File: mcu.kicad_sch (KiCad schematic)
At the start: 33 parts, among them J11 Conn_02x05_Odd_Even, J2 Conn_01x10, J3 Conn_01x10, J4 Conn_02x05_Odd_Even, U5 REF3033, U7 STM32F407VGTx, Y1 8MHz

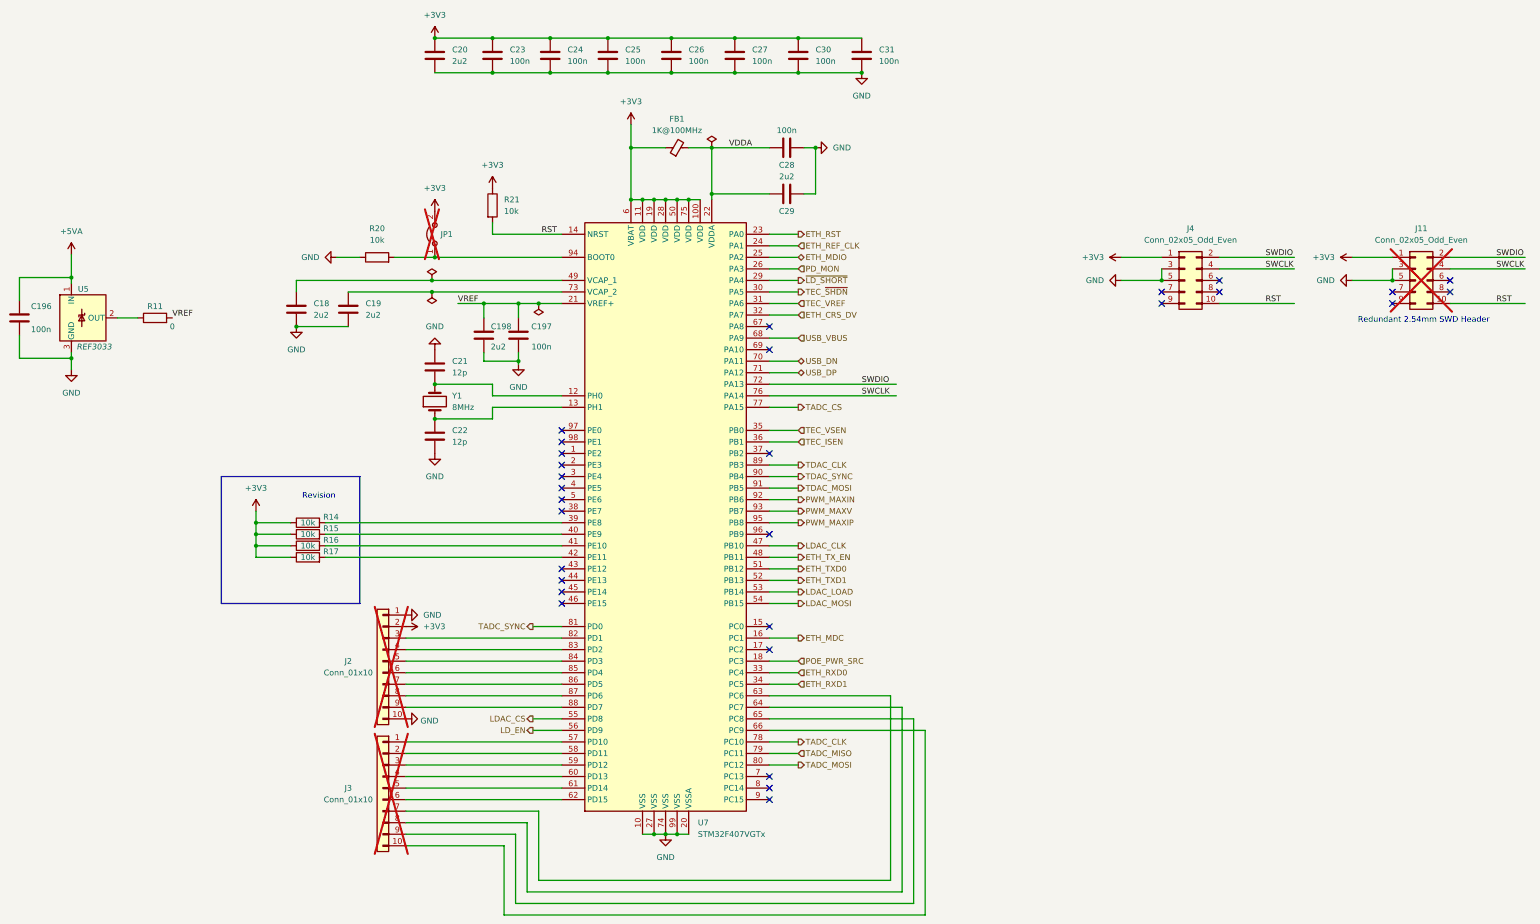
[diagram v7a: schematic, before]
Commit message: pcb: Finish Layout for rev0_3 - Assign MFR_PN for all Components - schematics changes:   - drivestage: Add Switch to optionally enable Modulation Signal Termination   -             Add alternate Precision Power Resistor   -             Modify the RC network values at TIA LPF Output   - MCU: Add Redundant 2.54mm pitch Programming Header   - thermostat: Duplicate the power filter network for alternate Temperature ADC
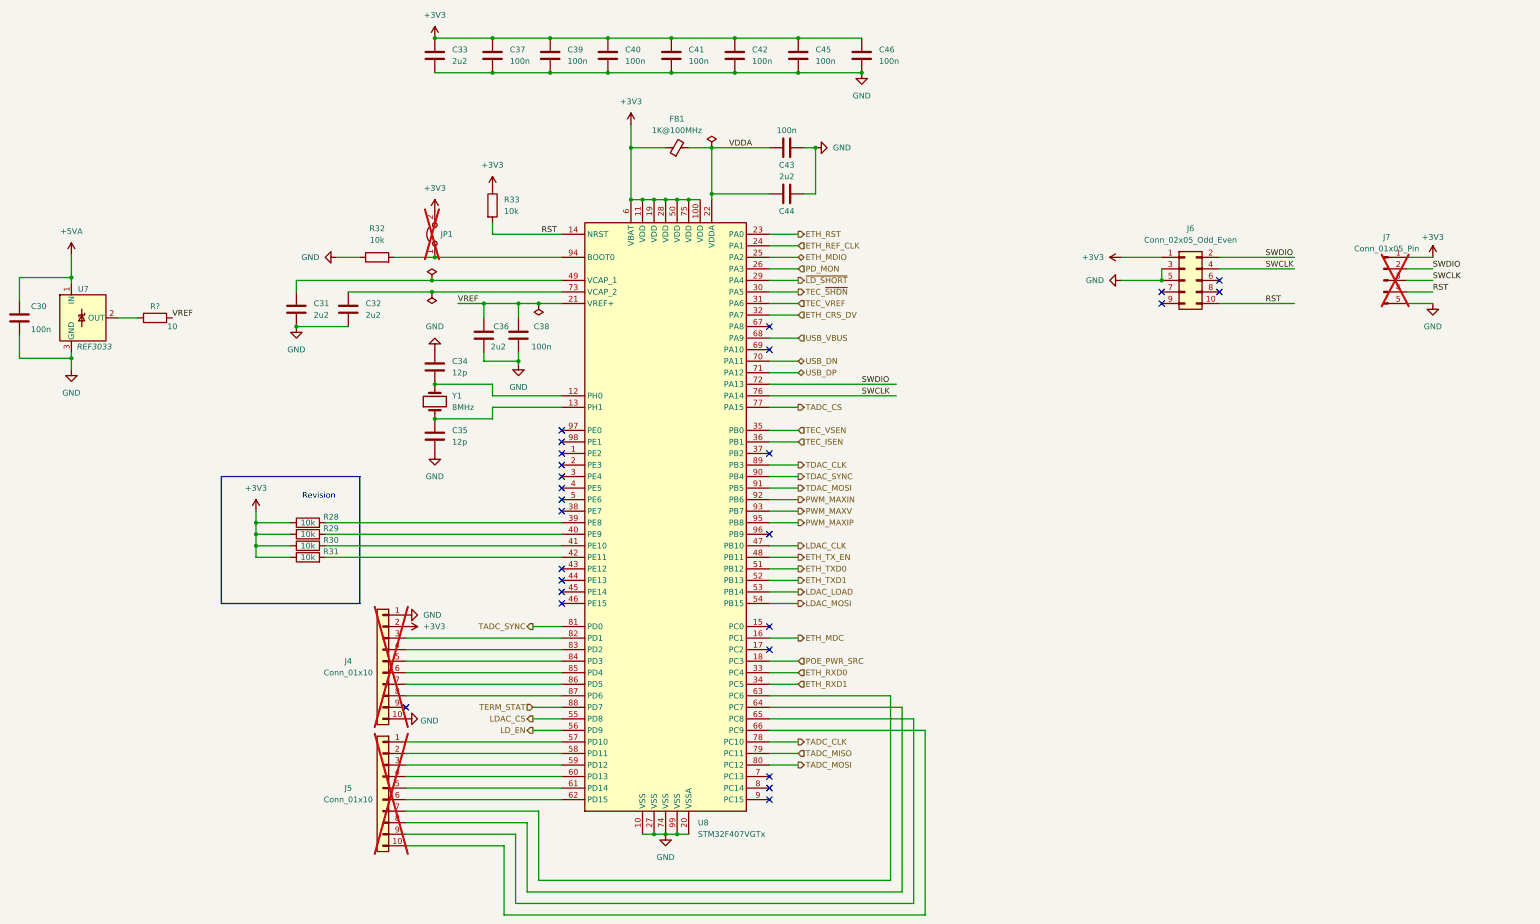
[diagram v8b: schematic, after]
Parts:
- removed J11: Conn_02x05_Odd_Even, Connector_PinHeader_2.54mm:PinHeader_2x05_P2.54mm_Vertical, symbol Connector_Generic:Conn_02x05_Odd_Even
- added J7: Conn_01x05_Pin, Connector_PinHeader_2.54mm:PinHeader_1x05_P2.54mm_Vertical, symbol Connector:Conn_01x05_Pin
- R?: renamed from R11; value 0 -> 10; MFR_PN RMCF0603ZT0R00 -> RT0603BRD0710RL; MFR_PN_ALT CR0603-J/-000ELF -> WR06X10R0FTL
- renumbered C196 to C30, C18 to C31, C19 to C32, C20 to C33, C21 to C34, C22 to C35, C198 to C36, C23 to C37, C197 to C38, C24 to C39, C25 to C40, C26 to C41, C27 to C42, C28 to C43, C29 to C44, C30 to C45, C31 to C46, J2 to J4, J3 to J5, J4 to J6, R14 to R28, R15 to R29, R16 to R30, R17 to R31, R20 to R32, R21 to R33, U5 to U7, U7 to U8
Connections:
- net +3V3: now also J7.1 (Pin_1)
- net GND: now also J7.5 (Pin_5)
- net RST: now also J7.4 (Pin_4)
- net SWCLK: now also J7.3 (Pin_3)
- net SWDIO: now also J7.2 (Pin_2)
- net at J4.9 (Pin_9): no longer U8.88 (PD7)
- new net TERM_STAT: U8.88 (PD7)
- no-connect marks 29 -> 26
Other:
- note removed: "Redundant 2.54mm SWD Header"
